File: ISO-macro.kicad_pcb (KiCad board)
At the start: 2 copper layers, 105.9 x 38.1 mm, 26 parts, among them J1 USB_C_Receptacle_USB2.0, SW1 SW_SPST, SW2 SW_SPST, SW3 SW_SPST, SW4 SW_SPST, SW5 SW_SPST, SW6 SW_SPST, SW7 SW_SPST, SW8 EC11, SW9 SW_SPST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

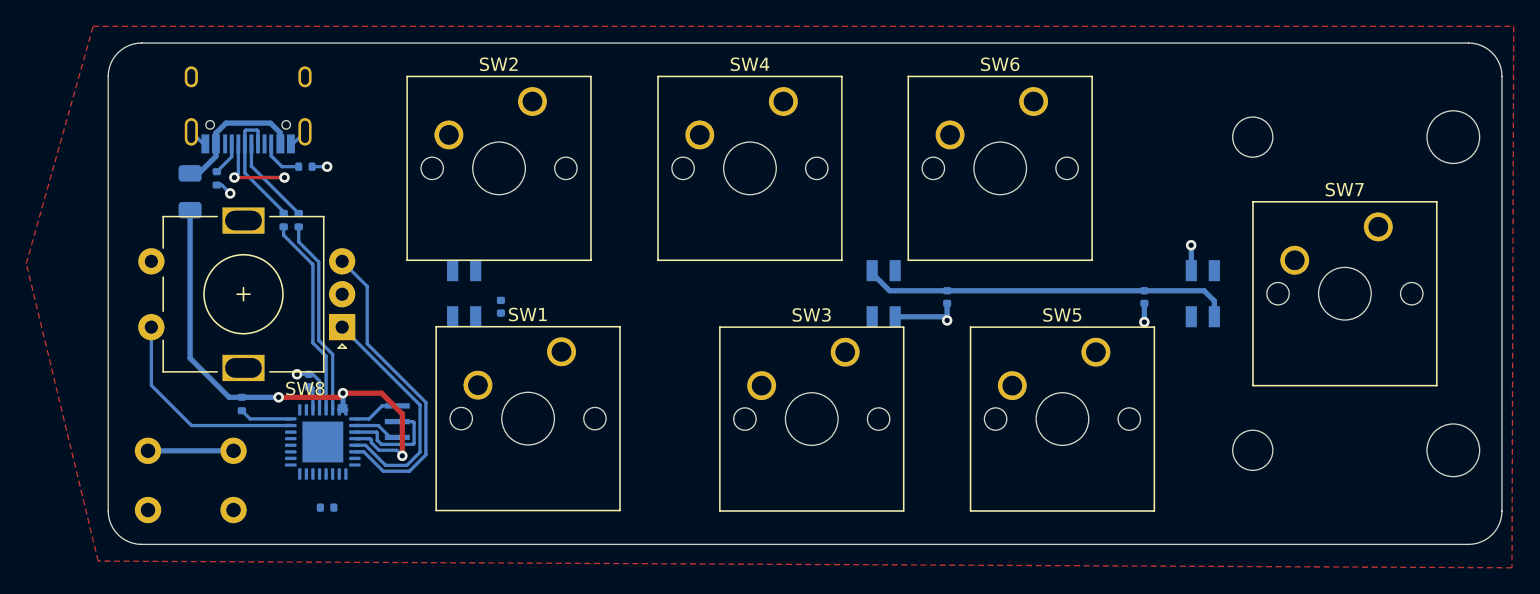
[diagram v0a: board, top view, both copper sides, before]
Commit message: Add LEDs and power caps, routing
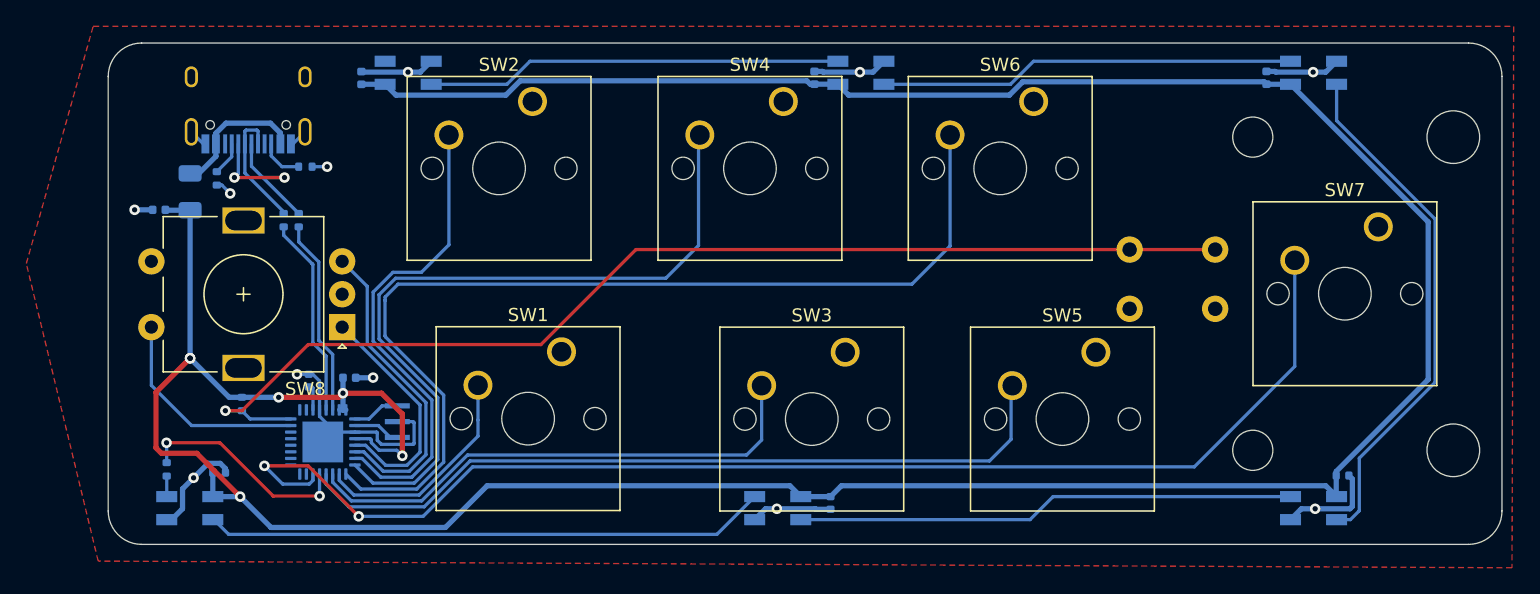
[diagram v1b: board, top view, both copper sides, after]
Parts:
- added C2: 100nF, Capacitor_SMD:C_0402_1005Metric, B.Cu at (128.5, 60.9)
- added C3: 100nF, Capacitor_SMD:C_0402_1005Metric, B.Cu at (197.2, 60.9)
- added C7: 100nF, Capacitor_SMD:C_0402_1005Metric, B.Cu at (162.9, 60.9)
- added C8: 10uF, Capacitor_SMD:C_0402_1005Metric, B.Cu at (113.1, 71.0)
- added C9: 100nF, Capacitor_SMD:C_0402_1005Metric, B.Cu at (127.5, 83.7)
- added D4: WS2812B, LED_SMD:LED_SK6812MINI_PLCC4_3.5x3.5mm_P1.75mm, B.Cu at (200.8, 60.6)
- added D5: WS2812B, LED_SMD:LED_SK6812MINI_PLCC4_3.5x3.5mm_P1.75mm, B.Cu at (166.4, 60.6)
- added D6: WS2812B, LED_SMD:LED_SK6812MINI_PLCC4_3.5x3.5mm_P1.75mm, B.Cu at (132.0, 60.6)
- moved SW9 76.1 mm to (193.3, 74.0)
- moved C5 33.0 mm to (203.0, 91.2), turned to 0 degrees
- moved C6 28.5 mm to (164.1, 93.2)
- moved D1 26.5 mm to (115.4, 93.6), turned to 180 degrees
- moved C4 24.9 mm to (117.7, 90.9), turned to 0 degrees
- moved D3 18.3 mm to (200.8, 93.6), turned to 180 degrees
- moved D2 18.2 mm to (160.1, 93.6), turned to 180 degrees
- moved R4 12.5 mm to (113.7, 90.7), turned to 90 degrees
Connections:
- J1 pad A8: Net-(J1-PadA8) -> (no net)
- J1 pad B8: Net-(J1-PadB8) -> (no net)
- SW1 pad 1: Net-(SW1-Pad1) -> GND
- SW2 pad 1: Net-(SW2-Pad1) -> GND
- SW3 pad 1: Net-(SW3-Pad1) -> GND
- SW4 pad 1: Net-(SW4-Pad1) -> GND
- SW5 pad 1: Net-(SW5-Pad1) -> GND
- SW6 pad 1: Net-(SW6-Pad1) -> GND
- SW7 pad 1: Net-(SW7-Pad1) -> GND
- U1 pad 10: Net-(U1-Pad10) -> Net-(SW1-Pad2)
- U1 pad 11: Net-(U1-Pad11) -> Net-(SW3-Pad2)
- U1 pad 12: Net-(U1-Pad12) -> Net-(SW5-Pad2)
- U1 pad 14: Net-(U1-Pad14) -> Net-(SW7-Pad2)
- U1 pad 15: Net-(U1-Pad15) -> (no net)
- U1 pad 16: Net-(SW4-Pad2) -> (no net)
- U1 pad 17: Net-(U1-Pad17) -> (no net)
- U1 pad 18: Net-(U1-Pad18) -> (no net)
- U1 pad 19: Net-(U1-Pad19) -> (no net)
- U1 pad 20: Net-(U1-Pad20) -> (no net)
- U1 pad 21: Net-(U1-Pad21) -> (no net)
- U1 pad 22: Net-(U1-Pad22) -> (no net)
- U1 pad 25: Net-(U1-Pad25) -> (no net)
- U1 pad 26: Net-(U1-Pad26) -> (no net)
- U1 pad 7: Net-(U1-Pad7) -> Net-(SW2-Pad2)
- U1 pad 8: Net-(U1-Pad8) -> Net-(SW4-Pad2)
- U1 pad 9: Net-(U1-Pad9) -> Net-(SW6-Pad2)
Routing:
- net VCC: track 66.9 -> 258.9 mm, vias 3 -> 6
- net Net-(SW7-Pad2): track 0.00 -> 97.5 mm, vias 0 -> 2
- net Net-(SW6-Pad2): track 0.00 -> 76.1 mm
- net /Reset: track 10.5 -> 85.5 mm, vias 0 -> 1
- net Net-(SW5-Pad2): track 0.00 -> 59.8 mm
- net Net-(SW4-Pad2): track 0.00 -> 56.3 mm
- net Net-(D1-Pad2): track 0.00 -> 42.8 mm
- net Net-(D3-Pad2): track 0.00 -> 39.9 mm
- net Net-(SW3-Pad2): track 0.00 -> 39.9 mm
- net Net-(D2-Pad2): track 0.00 -> 37.9 mm
- net Net-(SW2-Pad2): track 0.00 -> 37.1 mm
- net GND: track 26.2 -> 62.2 mm, vias 6 -> 11
- net Net-(D4-Pad2): track 0.00 -> 31.6 mm
- net Net-(D5-Pad2): track 0.00 -> 31.6 mm
- net Net-(SW1-Pad2): track 0.00 -> 17.2 mm
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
